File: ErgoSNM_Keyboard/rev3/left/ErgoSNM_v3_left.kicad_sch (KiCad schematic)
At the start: 23 parts, among them J1 USB_C_Receptacle_USB2.0, J2 Conn_01x04, J3 Conn_01x02, J4 Conn_01x08, SW1 SW_DPDT_x2, U1 RT9013-33GB, U4 TPS61220DCK

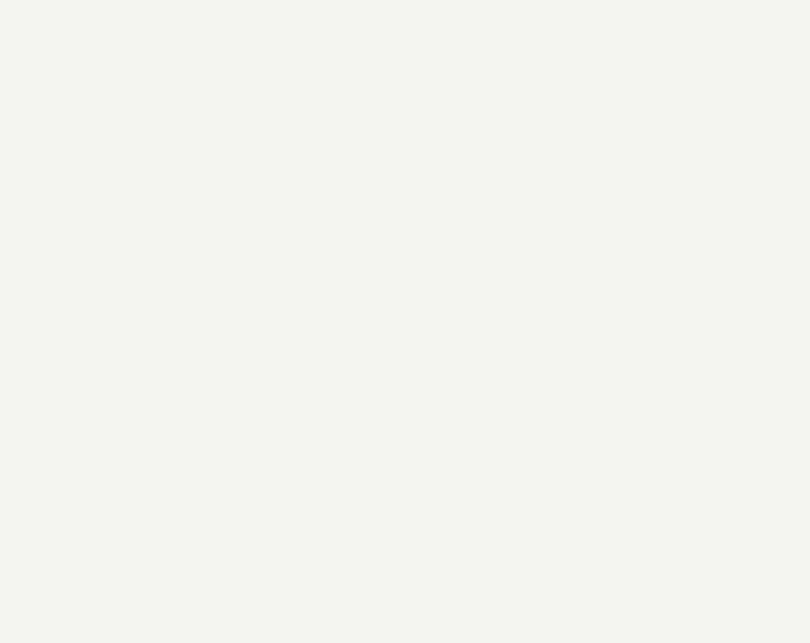
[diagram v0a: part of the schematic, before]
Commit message: Add key-matrix test pointes (2.54mm pin header)
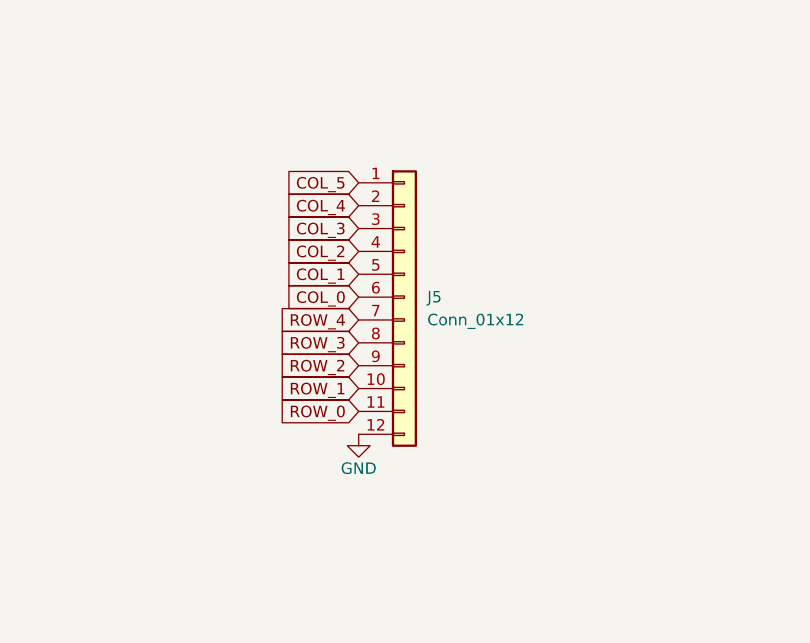
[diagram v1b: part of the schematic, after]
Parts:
- added J5: Conn_01x12, Connector_PinHeader_2.54mm:PinHeader_1x12_P2.54mm_Vertical, symbol Connector_Generic:Conn_01x12
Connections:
- net COL_5: now also J5.1 (Pin_1)
- net GND: now also J5.12 (Pin_12)
- net ROW_4: now also J5.7 (Pin_7)
- new net COL_0: J5.6 (Pin_6)
- new net COL_1: J5.5 (Pin_5)
- new net COL_2: J5.4 (Pin_4)
- new net COL_3: J5.3 (Pin_3)
- new net COL_4: J5.2 (Pin_2)
- new net ROW_0: J5.11 (Pin_11)
- new net ROW_1: J5.10 (Pin_10)
- new net ROW_2: J5.9 (Pin_9)
- new net ROW_3: J5.8 (Pin_8)

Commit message: Update submodule
Update submodule

Update switch footprint
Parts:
- renumbered C5 to C3, C6 to C4, J3 to J2, J2 to J3, U4 to U2
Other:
- moved on the sheet: J4, J5
